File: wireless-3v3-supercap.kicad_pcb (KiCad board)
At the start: 2 copper layers, 88 x 40 mm, 18 parts, among them J1 POWER-OUT, J2 POWER-IN, SW1 MODE, U1 BQ24640RVAR, U2 TPS61022

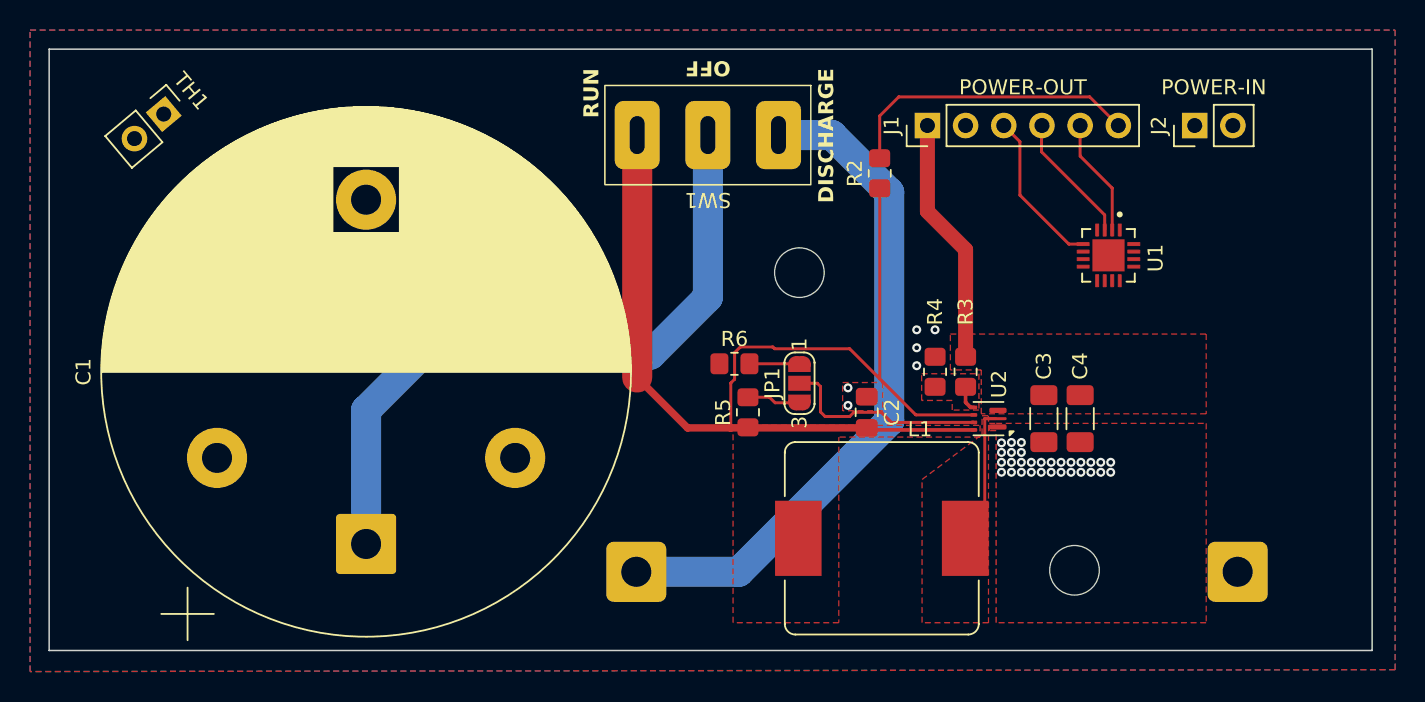
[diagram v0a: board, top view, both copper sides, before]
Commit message: Prefix all of the references so that the numbering is manageable across multiple circuits
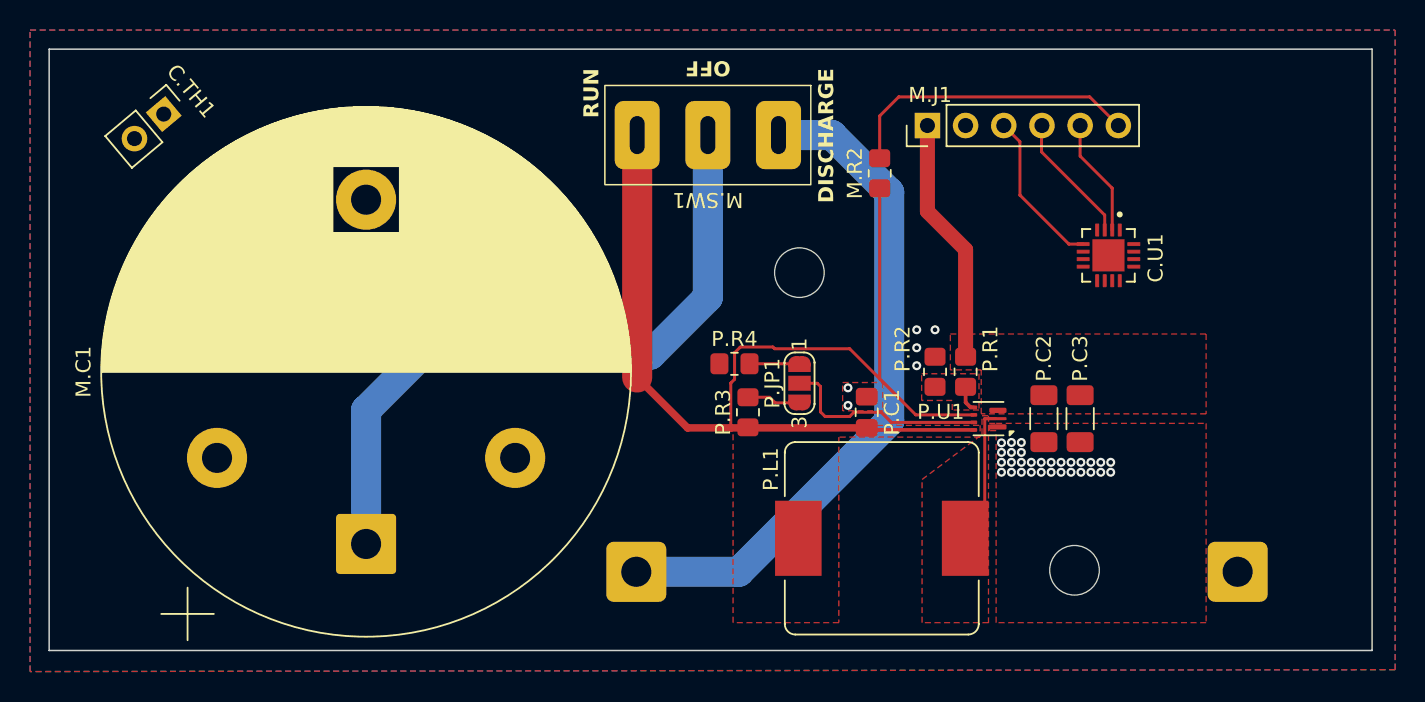
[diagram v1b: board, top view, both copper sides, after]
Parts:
- removed J2: POWER-IN, Connector_PinHeader_2.54mm:PinHeader_1x02_P2.54mm_Vertical
- renumbered TH1 to C.TH1, U1 to C.U1, C1 to M.C1, J1 to M.J1, R1 to M.R1, R2 to M.R2, SW1 to M.SW1, C2 to P.C1, C3 to P.C2, C4 to P.C3, JP1 to P.JP1, L1 to P.L1, R3 to P.R1, R4 to P.R2, R5 to P.R3, R6 to P.R4, U2 to P.U1

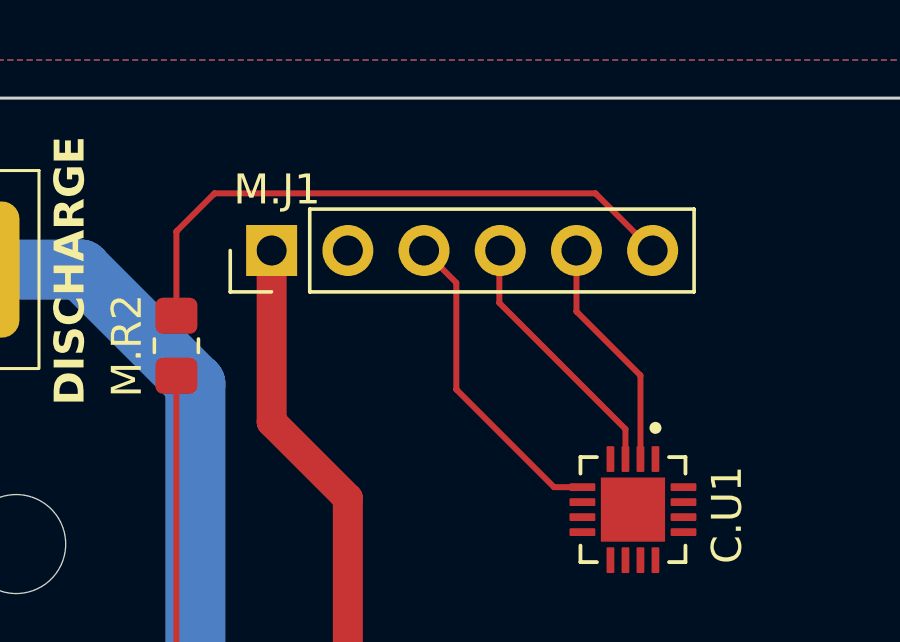
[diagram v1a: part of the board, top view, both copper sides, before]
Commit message: Remove charge enable pin
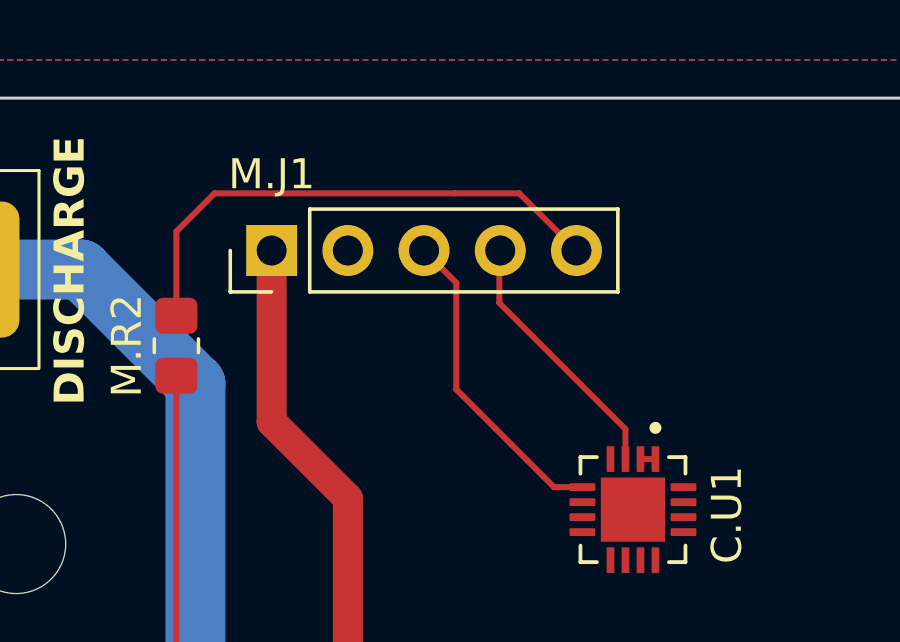
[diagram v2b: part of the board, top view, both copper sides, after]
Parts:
- M.J1: footprint Connector_PinHeader_2.54mm:PinHeader_1x06_P2.54mm_Vertical -> Connector_PinHeader_2.54mm:PinHeader_1x05_P2.54mm_Vertical
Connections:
- C.TH1 pad 1: unconnected-(C.TH1-Pad1) -> (no net)
- C.TH1 pad 2: unconnected-(C.TH1-Pad2) -> (no net)
- C.U1 pad 1: unconnected-(C.U1-VCC-Pad1) -> Net-(C.U1-CE)
- C.U1 pad 2: CHARGE_ENABLE -> Net-(C.U1-CE)
- M.J1 pad 5: CHARGE_ENABLE -> CAPACITOR_VOLTAGE
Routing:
- net CHARGE_ENABLE: track 7.84 -> 0.00 mm
- net CAPACITOR_VOLTAGE: track 20.0 -> 17.5 mm
- net Net-(C.U1-CE): track 0.00 -> 0.50 mm

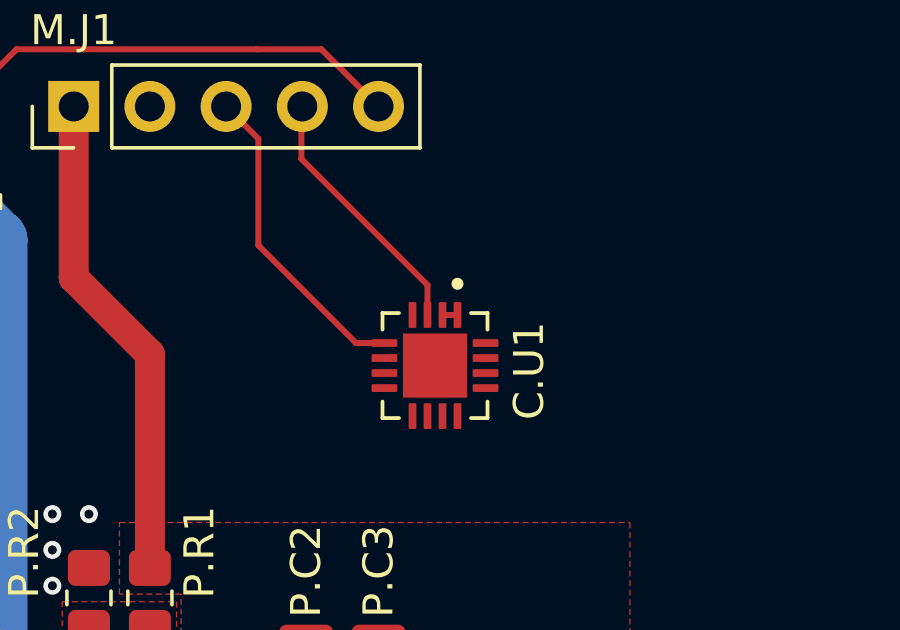
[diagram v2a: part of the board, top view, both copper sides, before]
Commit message: Connect charger CE to VREF, not VCC
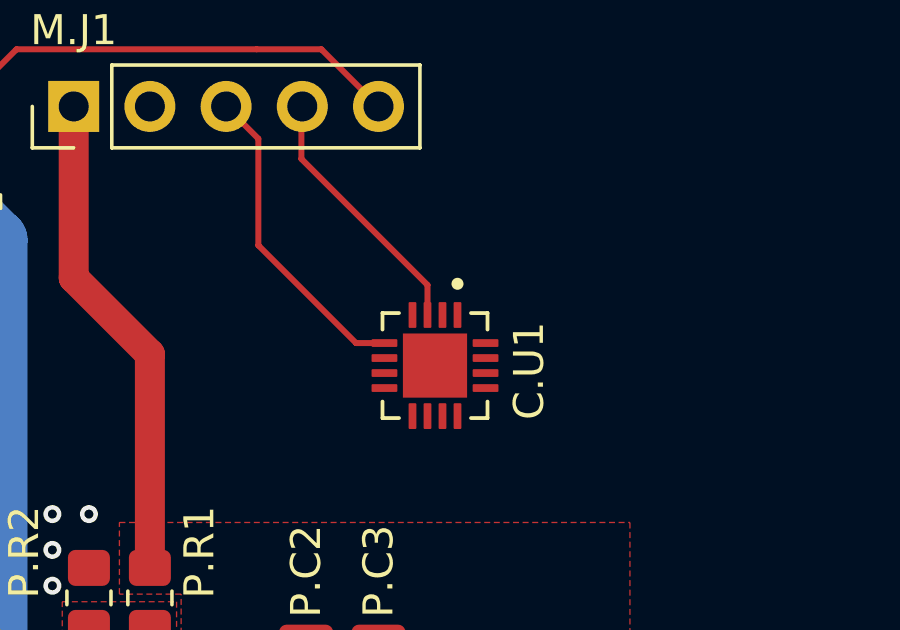
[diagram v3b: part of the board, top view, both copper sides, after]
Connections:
- C.U1 pad 1: Net-(C.U1-CE) -> unconnected-(C.U1-VCC-Pad1)
- C.U1 pad 11: unconnected-(C.U1-GND-Pad11) -> GND
- C.U1 pad 6: unconnected-(C.U1-VREF-Pad6) -> Net-(C.U1-CE)
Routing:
- net Net-(C.U1-CE): track 0.50 -> 0.00 mm
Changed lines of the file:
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@@
 	(net 12 "unconnected-(C.U1-EP-Pad17)")
 	(net 13 "unconnected-(C.U1-LODRV-Pad13)")
-	(net 14 "unconnected-(C.U1-VREF-Pad6)")
-	(net 15 "unconnected-(C.U1-SRN-Pad9)")
-	(net 16 "unconnected-(C.U1-TS-Pad4)")
-	(net 17 "unconnected-(C.U1-HIDRV-Pad15)")
-	(net 18 "unconnected-(C.U1-BTST-Pad16)")
-	(net 19 "unconnected-(C.U1-SRP-Pad10)")
-	(net 20 "unconnected-(C.U1-PH-Pad14)")
-	(net 21 "unconnected-(C.U1-GND-Pad11)")
-	(net 22 "unconnected-(C.U1-REGN-Pad12)")
-	(net 23 "unconnected-(C.U1-VFB-Pad8)")
-	(net 24 "Net-(P.JP1-B)")
-	(net 25 "Net-(P.JP1-C)")
-	(net 26 "Net-(P.JP1-A)")
-	(net 27 "Net-(C.U1-CE)")
+	(net 14 "unconnected-(C.U1-SRN-Pad9)")
+	(net 15 "unconnected-(C.U1-TS-Pad4)")
+	(net 16 "unconnected-(C.U1-HIDRV-Pad15)")
+	(net 17 "unconnected-(C.U1-BTST-Pad16)")
+	(net 18 "unconnected-(C.U1-SRP-Pad10)")
+	(net 19 "unconnected-(C.U1-PH-Pad14)")
+	(net 20 "unconnected-(C.U1-REGN-Pad12)")
+	(net 21 "unconnected-(C.U1-VFB-Pad8)")
+	(net 22 "Net-(P.JP1-B)")
+	(net 23 "Net-(P.JP1-C)")
+	(net 24 "Net-(P.JP1-A)")
+	(net 25 "Net-(C.U1-CE)")
+	(net 26 "unconnected-(C.U1-VCC-Pad1)")
 	(footprint "Resistor_SMD:R_0805_2012Metric_Pad1.20x1.40mm_HandSolder"
 		(layer "F.Cu")
@@
 			(layers "F.Cu" "F.Mask" "F.Paste")
 			(roundrect_rratio 0.208333)
-			(net 24 "Net-(P.JP1-B)")
+			(net 22 "Net-(P.JP1-B)")
 			(pintype "passive")
 		)
@@
 			(layers "F.Cu" "F.Mask" "F.Paste")
 			(roundrect_rratio 0.25)
-			(net 25 "Net-(P.JP1-C)")
+			(net 23 "Net-(P.JP1-C)")
 			(pinfunction "MODE")
 			(pintype "input")
@@
 			(layers "F.Cu" "F.Mask" "F.Paste")
 			(roundrect_rratio 0.125)
-			(net 27 "Net-(C.U1-CE)")
+			(net 26 "unconnected-(C.U1-VCC-Pad1)")
 			(pinfunction "VCC")
 			(pintype "power_in")
@@
 			(layers "F.Cu" "F.Mask" "F.Paste")
 			(roundrect_rratio 0.125)
-			(net 27 "Net-(C.U1-CE)")
+			(net 25 "Net-(C.U1-CE)")
 			(pinfunction "CE")
 			(pintype "input")
@@
 			(layers "F.Cu" "F.Mask" "F.Paste")
 			(roundrect_rratio 0.125)
-			(net 16 "unconnected-(C.U1-TS-Pad4)")
+			(net 15 "unconnected-(C.U1-TS-Pad4)")
 			(pinfunction "TS")
 			(pintype "input")
@@
 			(layers "F.Cu" "F.Mask" "F.Paste")
 			(roundrect_rratio 0.125)
-			(net 14 "unconnected-(C.U1-VREF-Pad6)")
+			(net 25 "Net-(C.U1-CE)")
 			(pinfunction "VREF")
 			(pintype "output")
@@
 			(layers "F.Cu" "F.Mask" "F.Paste")
 			(roundrect_rratio 0.125)
-			(net 23 "unconnected-(C.U1-VFB-Pad8)")
+			(net 21 "unconnected-(C.U1-VFB-Pad8)")
 			(pinfunction "VFB")
 			(pintype "input")
@@
 			(layers "F.Cu" "F.Mask" "F.Paste")
 			(roundrect_rratio 0.125)
-			(net 15 "unconnected-(C.U1-SRN-Pad9)")
+			(net 14 "unconnected-(C.U1-SRN-Pad9)")
 			(pinfunction "SRN")
 			(pintype "input")
@@
 			(layers "F.Cu" "F.Mask" "F.Paste")
 			(roundrect_rratio 0.125)
-			(net 19 "unconnected-(C.U1-SRP-Pad10)")
+			(net 18 "unconnected-(C.U1-SRP-Pad10)")
 			(pinfunction "SRP")
 			(pintype "input")
@@
 			(layers "F.Cu" "F.Mask" "F.Paste")
 			(roundrect_rratio 0.125)
-			(net 21 "unconnected-(C.U1-GND-Pad11)")
+			(net 1 "GND")
 			(pinfunction "GND")
 			(pintype "power_in")
@@
 			(layers "F.Cu" "F.Mask" "F.Paste")
 			(roundrect_rratio 0.125)
-			(net 22 "unconnected-(C.U1-REGN-Pad12)")
+			(net 20 "unconnected-(C.U1-REGN-Pad12)")
 			(pinfunction "REGN")
 			(pintype "output")
@@
 			(layers "F.Cu" "F.Mask" "F.Paste")
 			(roundrect_rratio 0.125)
-			(net 20 "unconnected-(C.U1-PH-Pad14)")
+			(net 19 "unconnected-(C.U1-PH-Pad14)")
 			(pinfunction "PH")
 			(pintype "power_in")
@@
 			(layers "F.Cu" "F.Mask" "F.Paste")
 			(roundrect_rratio 0.125)
-			(net 17 "unconnected-(C.U1-HIDRV-Pad15)")
+			(net 16 "unconnected-(C.U1-HIDRV-Pad15)")
 			(pinfunction "HIDRV")
 			(pintype "output")
@@
 			(layers "F.Cu" "F.Mask" "F.Paste")
 			(roundrect_rratio 0.125)
-			(net 18 "unconnected-(C.U1-BTST-Pad16)")
+			(net 17 "unconnected-(C.U1-BTST-Pad16)")
 			(pinfunction "BTST")
 			(pintype "power_in")
@@
 			(layers "F.Cu" "F.Mask" "F.Paste")
 			(roundrect_rratio 0.208333)
-			(net 26 "Net-(P.JP1-A)")
+			(net 24 "Net-(P.JP1-A)")
 			(pintype "passive")
 		)
@@
 			(size 1 0.5)
 			(layers "F.Cu" "F.Mask")
-			(net 26 "Net-(P.JP1-A)")
+			(net 24 "Net-(P.JP1-A)")
 			(pinfunction "A")
 			(pintype "passive")
@@
 			(size 1 1.5)
 			(layers "F.Cu" "F.Mask")
-			(net 25 "Net-(P.JP1-C)")
+			(net 23 "Net-(P.JP1-C)")
 			(pinfunction "C")
 			(pintype "passive")
@@
 			(size 1 0.5)
 			(layers "F.Cu" "F.Mask")
-			(net 24 "Net-(P.JP1-B)")
+			(net 22 "Net-(P.JP1-B)")
 			(pinfunction "B")
 			(pintype "passive")
@@
 		(width 0.2)
 		(layer "F.Cu")
-		(net 24)
+		(net 22)
 	)
 	(segment
@@
 		(width 0.2)
 		(layer "F.Cu")
-		(net 24)
+		(net 22)
 	)
 	(segment
@@
 		(width 0.2)
 		(layer "F.Cu")
-		(net 24)
+		(net 22)
 	)
 	(segment
@@
 		(width 0.2)
 		(layer "F.Cu")
-		(net 25)
+		(net 23)
 	)
 	(segment
@@
 		(width 0.2)
 		(layer "F.Cu")
-		(net 25)
+		(net 23)
 	)
 	(segment
@@
 		(width 0.2)
 		(layer "F.Cu")
-		(net 25)
+		(net 23)
 	)
 	(segment
@@
 		(width 0.2)
 		(layer "F.Cu")
-		(net 25)
+		(net 23)
 	)
 	(segment
@@
 		(width 0.2)
 		(layer "F.Cu")
-		(net 25)
+		(net 23)
 	)
 	(segment
@@
 		(width 0.2)
 		(layer "F.Cu")
-		(net 25)
+		(net 23)
 	)
 	(segment
@@
 		(width 0.2)
 		(layer "F.Cu")
-		(net 25)
+		(net 23)
 	)
 	(segment
@@
 		(width 0.2)
 		(layer "F.Cu")
-		(net 25)
+		(net 23)
 	)
 	(segment
@@
 		(width 0.2)
 		(layer "F.Cu")
-		(net 25)
+		(net 23)
 	)
 	(segment
@@
 		(width 0.2)
 		(layer "F.Cu")
-		(net 26)
-	)
-	(segment
-		(start 96.113526 37.432336)
-		(end 96.613526 37.432336)
-		(width 0.2)
-		(layer "F.Cu")
-		(net 27)
+		(net 24)
 	)
 	(zone

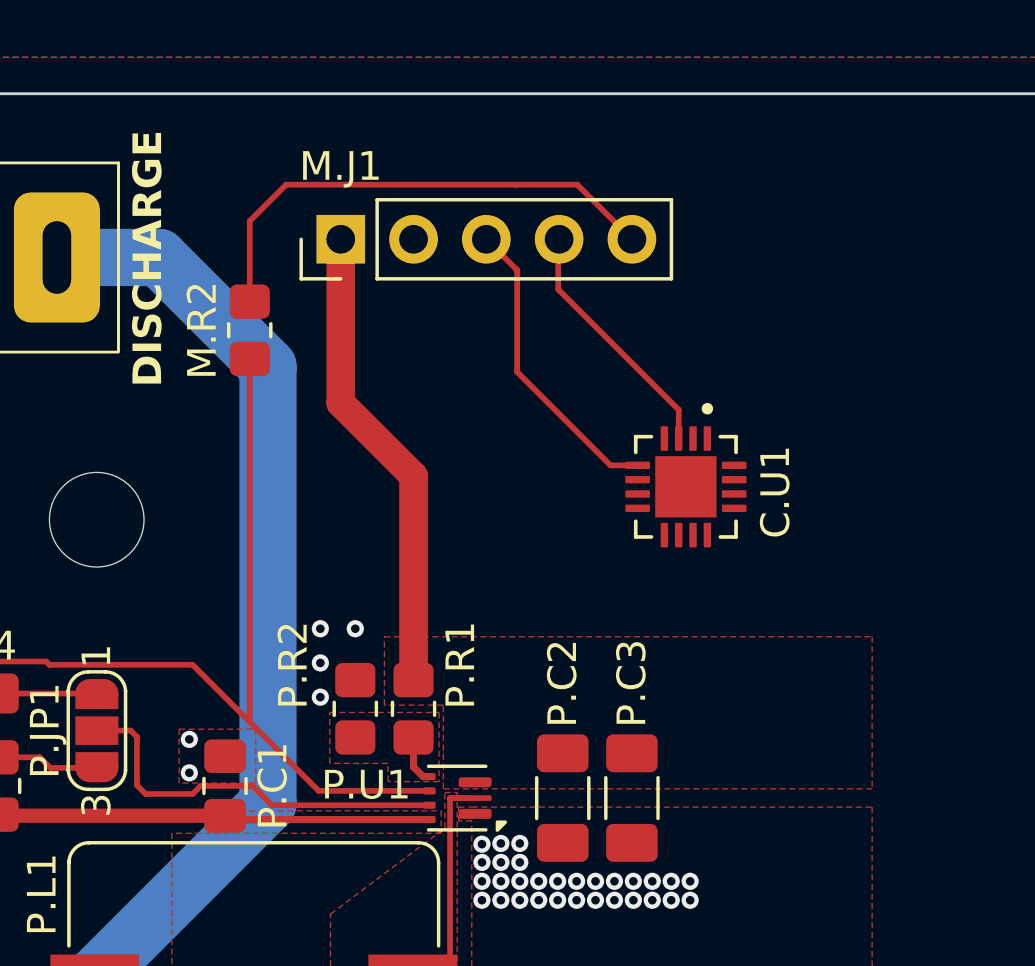
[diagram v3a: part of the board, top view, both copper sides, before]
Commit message: Add voltage divider circuit for ADC
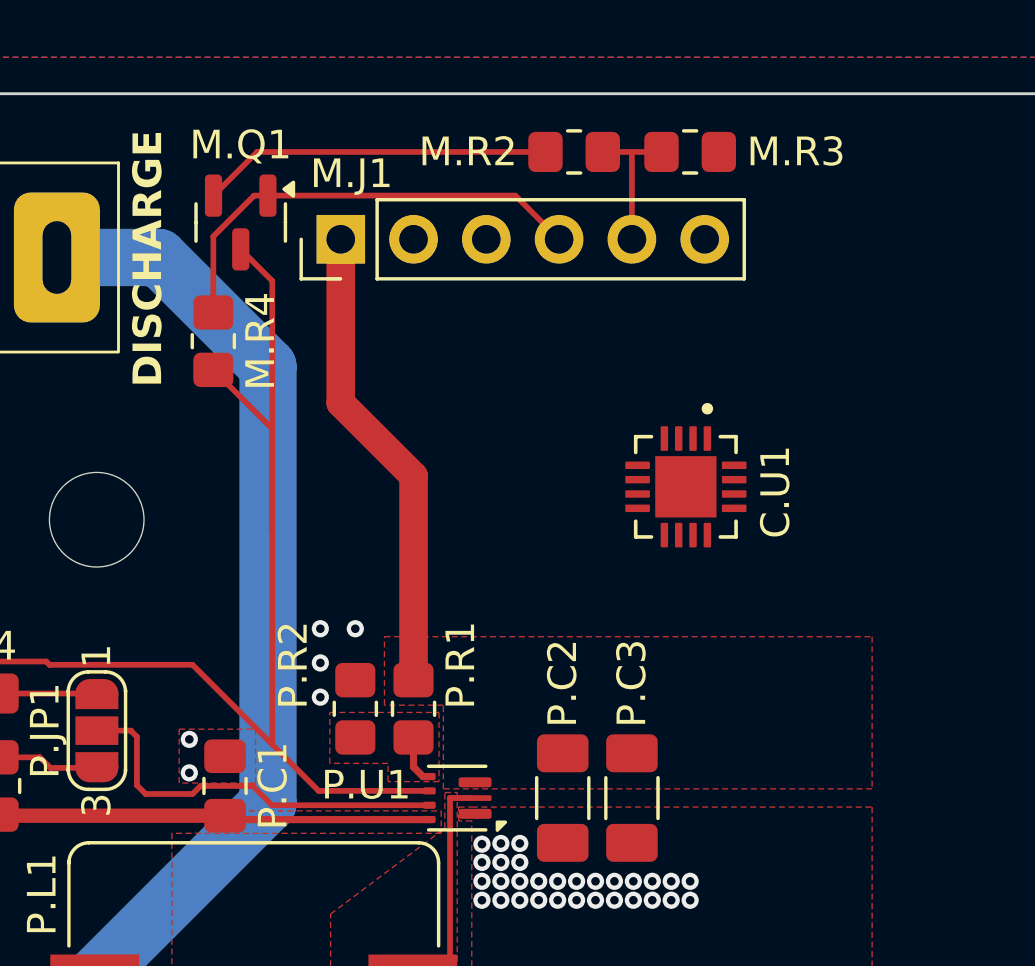
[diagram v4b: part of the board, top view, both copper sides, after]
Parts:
- added M.Q1: DMP2004K, Package_TO_SOT_SMD:SOT-23, F.Cu at (80.3, 29.9)
- added M.R3: 10kΩ 1% 125mW, Resistor_SMD:R_0805_2012Metric_Pad1.20x1.40mm_HandSolder, F.Cu at (96.0, 27.4)
- added M.R4: 10kΩ 1% 125mW, Resistor_SMD:R_0805_2012Metric_Pad1.20x1.40mm_HandSolder, F.Cu at (79.4, 34.0)
- M.J1: footprint Connector_PinHeader_2.54mm:PinHeader_1x05_P2.54mm_Vertical -> Connector_PinHeader_2.54mm:PinHeader_1x06_P2.54mm_Vertical
- M.R2: value 1kΩ 1% 125mW -> 26.1kΩ 1% 125mW
- P.R3, P.R4: value 10kΩ 125mW -> 10kΩ 1% 125mW
- moved M.R2 12.9 mm to (92.0, 27.4), turned to 0 degrees
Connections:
- C.TH1 pad 1: (no net) -> unconnected-(C.TH1-Pad1)
- C.TH1 pad 2: (no net) -> unconnected-(C.TH1-Pad2)
- M.J1 pad 2: GND -> EXTERNAL_POWER_PRESENT
- M.J1 pad 3: EXTERNAL_POWER_PRESENT -> CHARGE_STATUS
- M.J1 pad 4: CHARGE_STATUS -> MEASURE_VOLTAGE
- M.R2 pad 1: /Charge/SUPERCAP -> Net-(M.Q1-S)
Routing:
- net MEASURE_VOLTAGE: track 0.00 -> 15.9 mm
- net Net-(M.Q1-S): track 0.00 -> 13.2 mm
- net CAPACITOR_VOLTAGE: track 17.5 -> 5.10 mm
- net /Charge/SUPERCAP: track 75.5 -> 87.0 mm
- net EXTERNAL_POWER_PRESENT: track 10.6 -> 0.00 mm
- net CHARGE_STATUS: track 8.66 -> 0.00 mm
